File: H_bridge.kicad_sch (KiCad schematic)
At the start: 13 parts, among them M1 Motor_AC, Q1 AO3400A, Q2 AO3400A, Q3 AO3400A, Q4 AO3400A, U2 SLM2009, U3 SLM2009

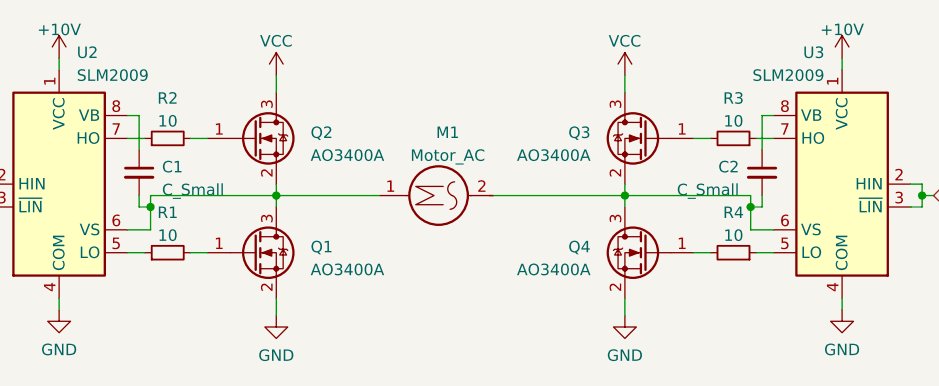
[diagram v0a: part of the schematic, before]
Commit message: mostek H, serva, SMPS
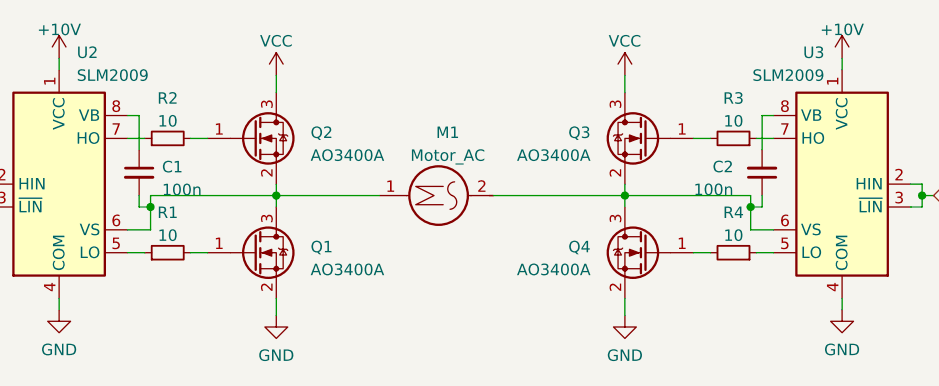
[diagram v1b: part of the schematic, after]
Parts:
- C1, C2: value C_Small -> 100n
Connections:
- net at M1.2, Q3.2 (S), Q4.3 (D)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: now also C2.1; no longer C2.2
- net at U3.8 (VB): now also C2.2; no longer C2.1
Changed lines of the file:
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@@
     )
   )
-  (symbol (lib_id "Device:C_Small") (at 172.085 83.82 0) (mirror y) (unit 1)
+  (symbol (lib_id "Device:C_Small") (at 172.085 83.82 0) (mirror x) (unit 1)
     (in_bom yes) (on_board yes) (dnp no) (fields_autoplaced)
-    (property "Reference" "C2" (at 169.545 83.1913 0)
-      (effects (font (size 1.27 1.27)) (justify left))
+    (property "Reference" "C2" (at 168.91 83.1786 0)
+      (effects (font (size 1.27 1.27)) (justify right))
     )
-    (property "Value" "C_Small" (at 169.545 85.7313 0)
-      (effects (font (size 1.27 1.27)) (justify left))
+    (property "Value" "100n" (at 168.91 85.7186 0)
+      (effects (font (size 1.27 1.27)) (justify right))
     )
     (property "Footprint" "" (at 172.085 83.82 0)
@@
       (effects (font (size 1.27 1.27)) (justify left))
     )
-    (property "Value" "C_Small" (at 105.41 85.7313 0)
+    (property "Value" "100n" (at 105.41 85.7313 0)
       (effects (font (size 1.27 1.27)) (justify left))
     )

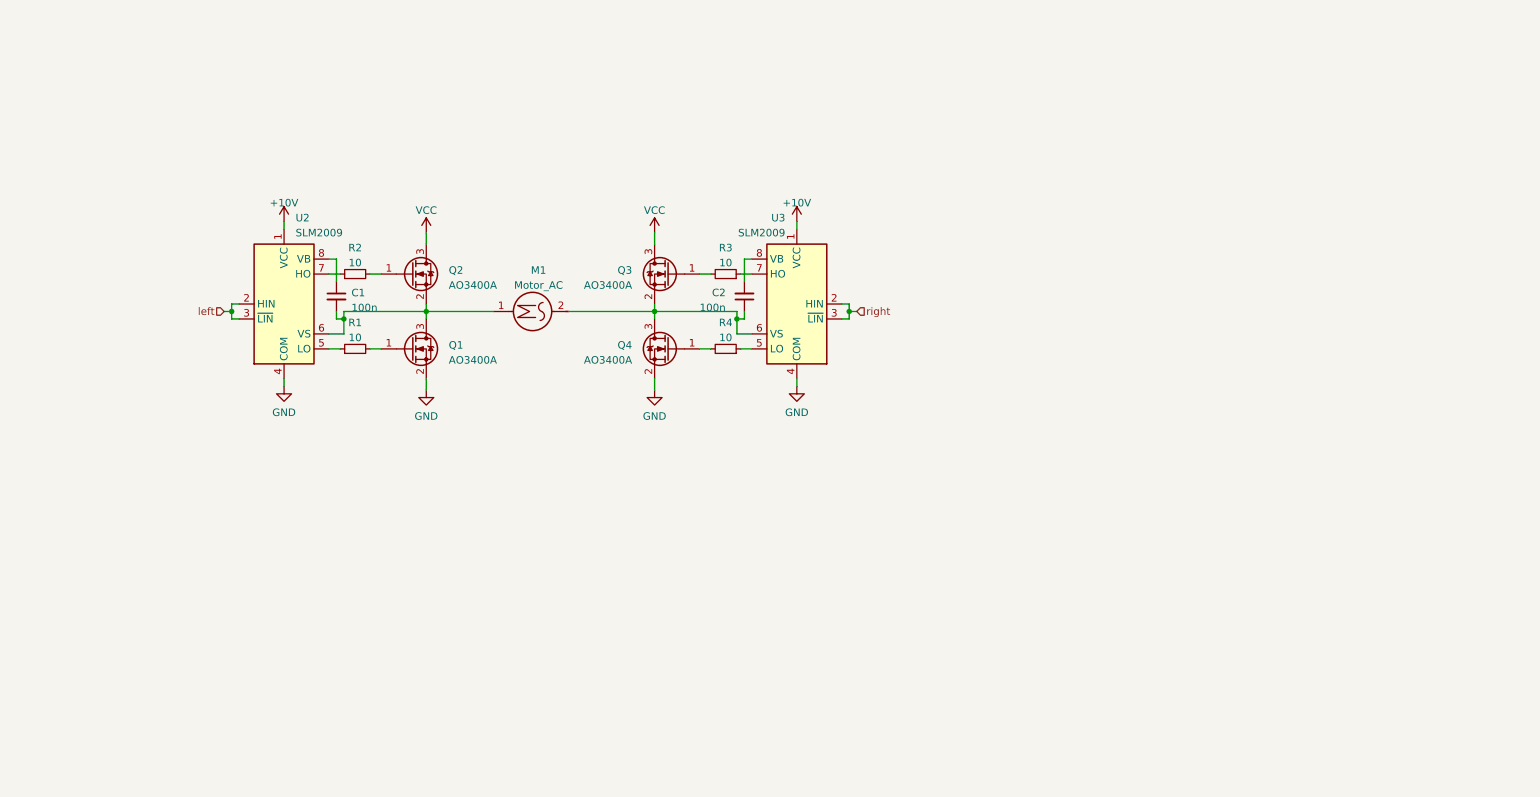
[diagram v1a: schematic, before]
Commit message: routing of H bridges and servo power pins
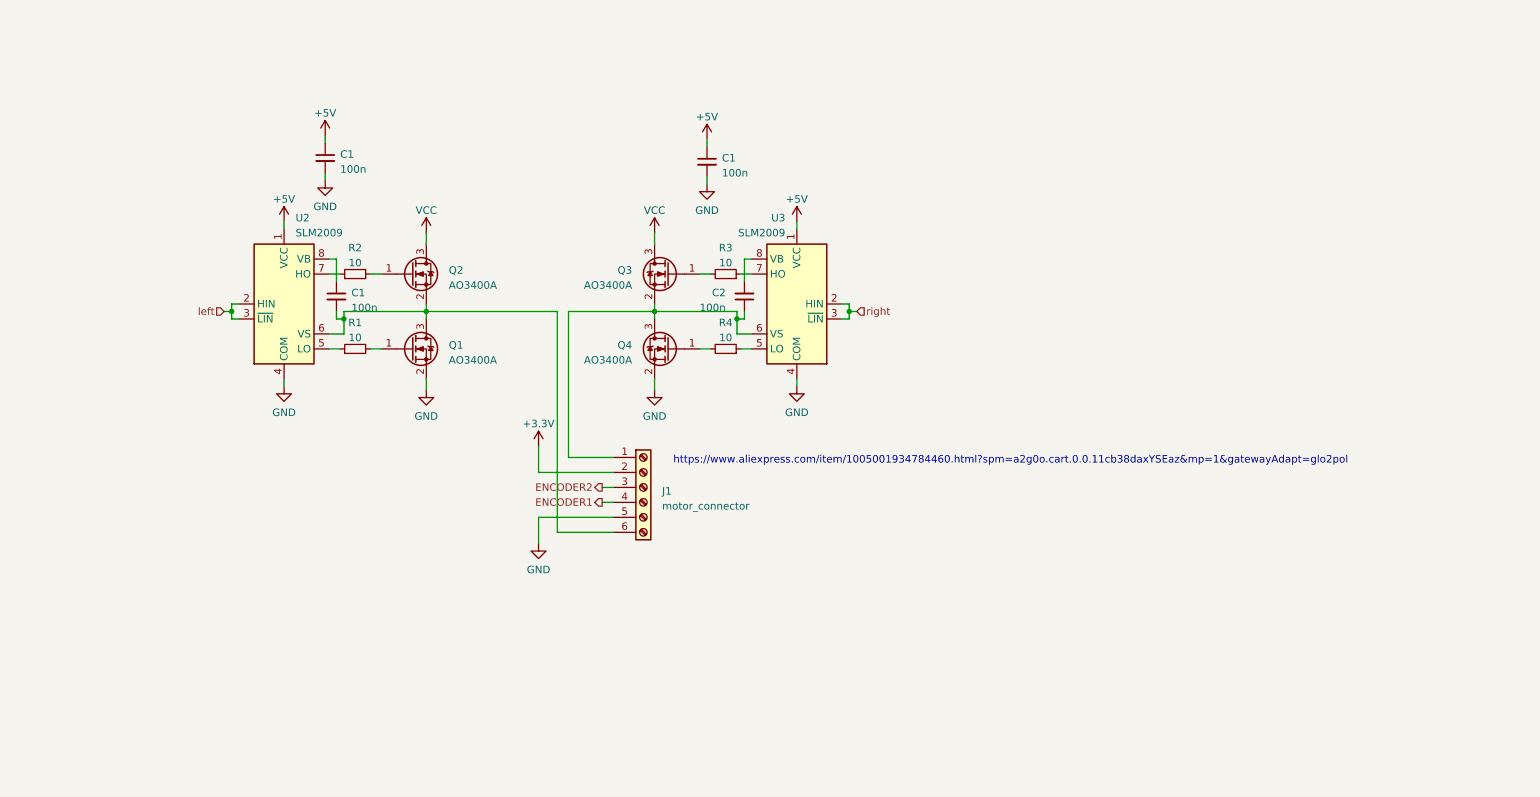
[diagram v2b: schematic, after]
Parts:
- removed M1: Motor_AC, symbol Motor:Motor_AC
- added C1 (x2): 100n, Capacitor_SMD:C_0603_1608Metric_Pad1.08x0.95mm_HandSolder, symbol Device:C_Small
- added J1: motor_connector, symbol Connector:Screw_Terminal_01x06
- C1, C2: footprint (none) -> Capacitor_SMD:C_0603_1608Metric_Pad1.08x0.95mm_HandSolder
- R1, R2, R3, R4: footprint (none) -> Resistor_SMD:R_0603_1608Metric_Pad0.98x0.95mm_HandSolder
- U2, U3: footprint (none) -> Package_SO:SOIC-8_3.9x4.9mm_P1.27mm
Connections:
- net GND: now also C1.2, C1.2, J1.5 (Pin_5)
- net at C1.2, Q1.3 (D), Q2.2 (S)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: now also J1.6 (Pin_6)
- net at C2.1, Q3.2 (S), Q4.3 (D)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: now also J1.1 (Pin_1)
- net +10V renamed +5V
- net +5V: now also C1.1, C1.1
- new net +3.3V: J1.2 (Pin_2)
- new net ENCODER1: J1.4 (Pin_4)
- new net ENCODER2: J1.3 (Pin_3)
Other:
- note added: "https://www.aliexpress.com/item/1005001934784460.html?spm=a2g0o.cart.0.0.11cb38daxYSEaz&mp=1&gatewayAdapt=glo2pol"

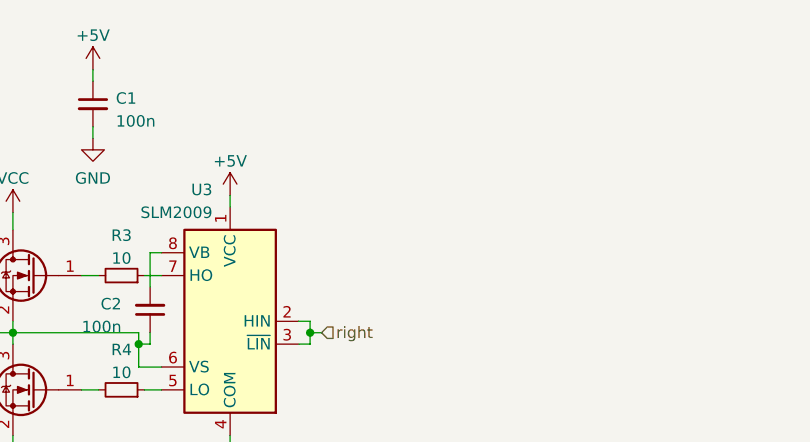
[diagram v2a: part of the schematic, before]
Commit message: more capacitance near motors 16x22uF total 3S->2S
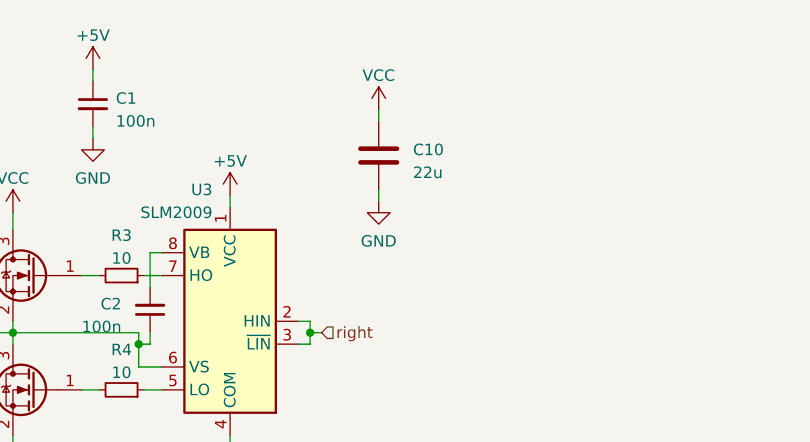
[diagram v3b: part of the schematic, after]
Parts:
- added C10: 22u, Capacitor_SMD:C_0805_2012Metric_Pad1.18x1.45mm_HandSolder, symbol Device:C
- J1: footprint (none) -> Connector_PinSocket_2.54mm:PinSocket_1x06_P2.54mm_Vertical
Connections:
- net GND: now also C10.2
- net VCC: now also C10.1
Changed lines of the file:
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@@
+    (stroke (width 0) (type default))
+  )
+  (wire (pts (xy 197.485 61.595) (xy 197.485 62.865))
     (stroke (width 0) (type default))
   )
@@
   )
   (wire (pts (xy 166.37 80.01) (xy 164.465 80.01))
+    (stroke (width 0) (type default))
+  )
+  (wire (pts (xy 197.485 70.485) (xy 197.485 71.755))
     (stroke (width 0) (type default))
   )
@@
       (effects (font (size 1.27 1.27)) (justify left))
     )
-    (property "Footprint" "" (at 154.94 116.205 0)
+    (property "Footprint" "Connector_PinSocket_2.54mm:PinSocket_1x06_P2.54mm_Vertical" (at 154.94 116.205 0)
       (effects (font (size 1.27 1.27)) hide)
     )
@@
     )
   )
+  (symbol (lib_id "Device:C") (at 197.485 66.675 0) (unit 1)
+    (in_bom yes) (on_board yes) (dnp no) (fields_autoplaced)
+    (property "Reference" "C10" (at 201.295 66.04 0)
+      (effects (font (size 1.27 1.27)) (justify left))
+    )
+    (property "Value" "22u" (at 201.295 68.58 0)
+      (effects (font (size 1.27 1.27)) (justify left))
+    )
+    (property "Footprint" "Capacitor_SMD:C_0805_2012Metric_Pad1.18x1.45mm_HandSolder" (at 198.4502 70.485 0)
+      (effects (font (size 1.27 1.27)) hide)
+    )
+    (property "Datasheet" "~" (at 197.485 66.675 0)
+      (effects (font (size 1.27 1.27)) hide)
+    )
+    (pin "1")
+    (pin "2")
+    (instances
+      (project "version_1"
+        (path "/23ba0750-4a55-4d50-828b-749cc0fbb8c8"
+          (reference "C10") (unit 1)
+        )
+        (path "/23ba0750-4a55-4d50-828b-749cc0fbb8c8/9789521c-7f58-473a-9dd2-6c6a71290f6c"
+          (reference "C15") (unit 1)
+        )
+        (path "/23ba0750-4a55-4d50-828b-749cc0fbb8c8/03ada194-765a-457e-8ab8-6dd2c4500630"
+          (reference "C35") (unit 1)
+        )
+        (path "/23ba0750-4a55-4d50-828b-749cc0fbb8c8/79f7122c-c2a5-4829-b847-ff54a5199600"
+          (reference "C36") (unit 1)
+        )
+        (path "/23ba0750-4a55-4d50-828b-749cc0fbb8c8/d2110296-333c-46f5-b5da-c8cbeafe02ed"
+          (reference "C37") (unit 1)
+        )
+        (path "/23ba0750-4a55-4d50-828b-749cc0fbb8c8/1b8f704b-b129-4c22-a423-d346d579d0e5"
+          (reference "C38") (unit 1)
+        )
+        (path "/23ba0750-4a55-4d50-828b-749cc0fbb8c8/0734ecc9-bf55-4847-b598-21bbdec71699"
+          (reference "C39") (unit 1)
+        )
+      )
+    )
+  )
   (symbol (lib_id "Transistor_FET:AO3400A") (at 159.385 80.01 0) (mirror y) (unit 1)
     (in_bom yes) (on_board yes) (dnp no) (fields_autoplaced)
@@
         (path "/23ba0750-4a55-4d50-828b-749cc0fbb8c8/0734ecc9-bf55-4847-b598-21bbdec71699"
           (reference "#PWR072") (unit 1)
+        )
+      )
+    )
+  )
+  (symbol (lib_id "power:GND") (at 197.485 71.755 0) (unit 1)
+    (in_bom yes) (on_board yes) (dnp no) (fields_autoplaced)
+    (property "Reference" "#PWR055" (at 197.485 78.105 0)
+      (effects (font (size 1.27 1.27)) hide)
+    )
+    (property "Value" "GND" (at 197.485 76.2 0)
+      (effects (font (size 1.27 1.27)))
+    )
+    (property "Footprint" "" (at 197.485 71.755 0)
+      (effects (font (size 1.27 1.27)) hide)
+    )
+    (property "Datasheet" "" (at 197.485 71.755 0)
+      (effects (font (size 1.27 1.27)) hide)
+    )
+    (pin "1")
+    (instances
+      (project "version_1"
+        (path "/23ba0750-4a55-4d50-828b-749cc0fbb8c8"
+          (reference "#PWR055") (unit 1)
+        )
+        (path "/23ba0750-4a55-4d50-828b-749cc0fbb8c8/9789521c-7f58-473a-9dd2-6c6a71290f6c"
+          (reference "#PWR066") (unit 1)
+        )
+        (path "/23ba0750-4a55-4d50-828b-749cc0fbb8c8/03ada194-765a-457e-8ab8-6dd2c4500630"
+          (reference "#PWR0117") (unit 1)
+        )
+        (path "/23ba0750-4a55-4d50-828b-749cc0fbb8c8/79f7122c-c2a5-4829-b847-ff54a5199600"
+          (reference "#PWR0119") (unit 1)
+        )
+        (path "/23ba0750-4a55-4d50-828b-749cc0fbb8c8/d2110296-333c-46f5-b5da-c8cbeafe02ed"
+          (reference "#PWR0121") (unit 1)
+        )
+        (path "/23ba0750-4a55-4d50-828b-749cc0fbb8c8/1b8f704b-b129-4c22-a423-d346d579d0e5"
+          (reference "#PWR0123") (unit 1)
+        )
+        (path "/23ba0750-4a55-4d50-828b-749cc0fbb8c8/0734ecc9-bf55-4847-b598-21bbdec71699"
+          (reference "#PWR0125") (unit 1)
         )
       )
@@
         )
       )
+    )
+  )
+  (symbol (lib_id "power:VCC") (at 197.485 61.595 0) (unit 1)
+    (in_bom yes) (on_board yes) (dnp no) (fields_autoplaced)
+    (property "Reference" "#PWR051" (at 197.485 65.405 0)
+      (effects (font (size 1.27 1.27)) hide)
+    )
+    (property "Value" "VCC" (at 197.485 57.785 0)
+      (effects (font (size 1.27 1.27)))
+    )
+    (property "Footprint" "" (at 197.485 61.595 0)
+      (effects (font (size 1.27 1.27)) hide)
+    )
+    (property "Datasheet" "" (at 197.485 61.595 0)
+      (effects (font (size 1.27 1.27)) hide)
+    )
+    (pin "1")
+    (instances
+      (project "version_1"
+        (path "/23ba0750-4a55-4d50-828b-749cc0fbb8c8"
+          (reference "#PWR051") (unit 1)
+        )
+        (path "/23ba0750-4a55-4d50-828b-749cc0fbb8c8/9789521c-7f58-473a-9dd2-6c6a71290f6c"
+          (reference "#PWR065") (unit 1)
+        )
+        (path "/23ba0750-4a55-4d50-828b-749cc0fbb8c8/03ada194-765a-457e-8ab8-6dd2c4500630"
+          (reference "#PWR0116") (unit 1)
+        )
+        (path "/23ba0750-4a55-4d50-828b-749cc0fbb8c8/79f7122c-c2a5-4829-b847-ff54a5199600"
+          (reference "#PWR0118") (unit 1)
+        )
+        (path "/23ba0750-4a55-4d50-828b-749cc0fbb8c8/d2110296-333c-46f5-b5da-c8cbeafe02ed"
+          (reference "#PWR0120") (unit 1)
+        )
+        (path "/23ba0750-4a55-4d50-828b-749cc0fbb8c8/1b8f704b-b129-4c22-a423-d346d579d0e5"
+          (reference "#PWR0122") (unit 1)
+        )
+        (path "/23ba0750-4a55-4d50-828b-749cc0fbb8c8/0734ecc9-bf55-4847-b598-21bbdec71699"
+          (reference "#PWR0124") (unit 1)
+        )
+      )

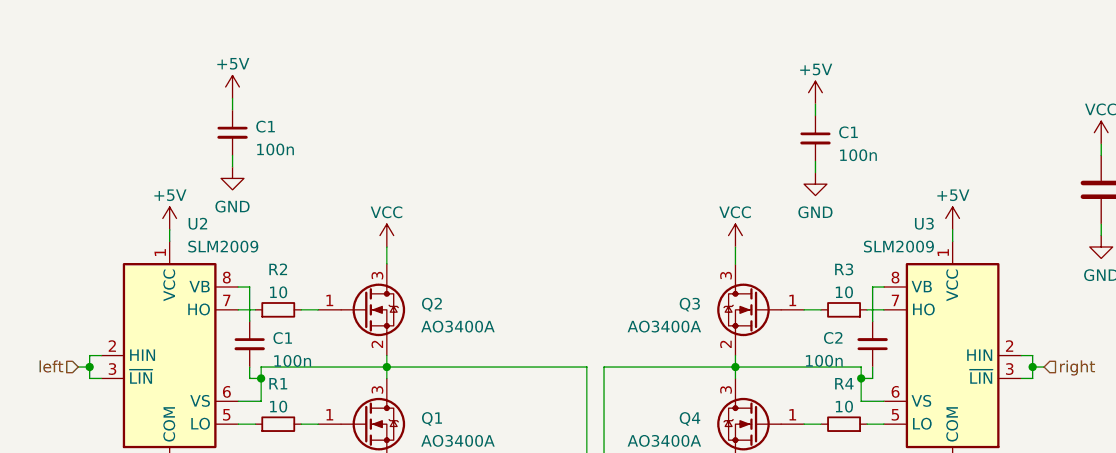
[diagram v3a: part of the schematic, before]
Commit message: new version of layout with diodes improved power routing a little bit
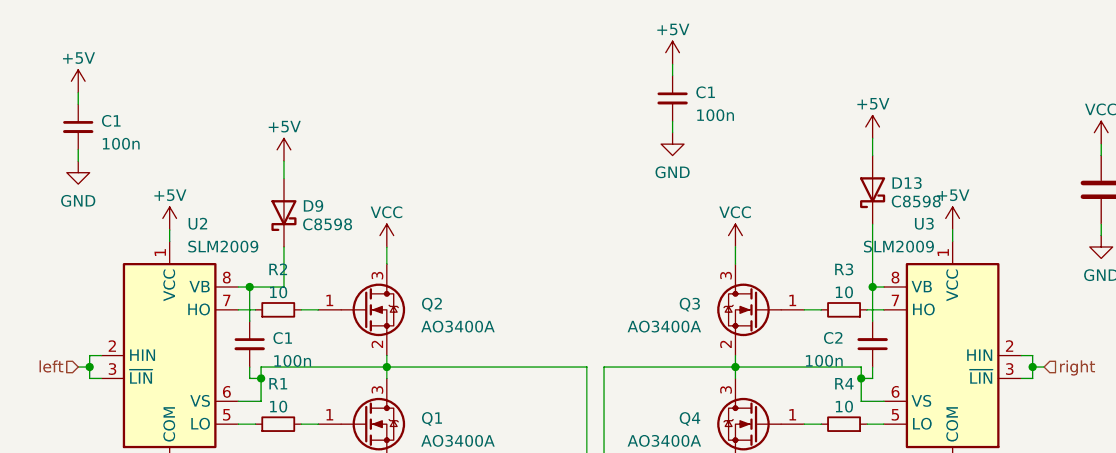
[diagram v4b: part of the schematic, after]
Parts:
- added D13, D9: C8598, Diode_SMD:D_SOD-123, symbol Device:D_Schottky
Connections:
- net +5V: now also D13.2 (A), D9.2 (A)
- net at C2.2, U3.8 (VB): now also D13.1 (K)
- net at C1.1, U2.8 (VB): now also D9.1 (K)
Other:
- moved on the sheet: C1

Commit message: added moany componaets
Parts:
- added C10 (x5): 22u, Capacitor_SMD:C_0805_2012Metric_Pad1.18x1.45mm_HandSolder, symbol Device:C
- added CN1: B6B-PH-K-S(LF)(SN), footprint:CONN-TH_B6B-PH-K-S, symbol B6B-PH-K-S(LF)(SN):B6B-PH-K-S(LF)(SN)
- added U13: DRV8870DDA, Package_SO:Texas_HTSOP-8-1EP_3.9x4.9mm_P1.27mm_EP2.95x4.9mm_Mask2.4x3.1mm_ThermalVias, symbol Driver_Motor:DRV8870DDA
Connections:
- net +3.3V: now also CN1.5
- net +5V: now also U13.4 (VREF)
- net GND: now also C10.2, C10.2, C10.2, C10.2, C10.2, U13.1 (GND), U13.7 (ISEN), U13.9 (GND)
- net VCC: now also C10.1, C10.1, C10.1, C10.1, C10.1, U13.5 (VM)
- net left: now also U13.3 (IN1)
- net right: now also U13.2 (IN2)
- new net: CN1.1, U13.8 (OUT2)
- new net: CN1.6, U13.6 (OUT1)
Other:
- note added: "C131342"

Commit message: some changes
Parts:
- removed C2: 100n, Capacitor_SMD:C_0603_1608Metric_Pad1.08x0.95mm_HandSolder, symbol Device:C_Small
- removed D13, D9: C8598, Diode_SMD:D_SOD-123, symbol Device:D_Schottky
- removed J1: motor_connector, Connector_PinSocket_2.54mm:PinSocket_1x06_P2.54mm_Vertical, symbol Connector:Screw_Terminal_01x06
- removed Q1, Q2, Q3, Q4: AO3400A, Package_TO_SOT_SMD:SOT-23, symbol Transistor_FET:AO3400A
- removed R1, R2, R3, R4: 10, Resistor_SMD:R_0603_1608Metric_Pad0.98x0.95mm_HandSolder, symbol Device:R_Small
- removed U2, U3: SLM2009, Package_SO:SOIC-8_3.9x4.9mm_P1.27mm, symbol Driver_FET:IR2103
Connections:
- net ENCODER1: now also CN1.3
- net ENCODER2: now also CN1.4
- net GND: now also C1.2, CN1.2
- net VCC: now also C1.1
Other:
- note added: "Need to flip?"
- note removed: "C131342"
- note removed: "https://www.aliexpress.com/item/1005001934784460.html?spm=a2g0o.cart.0.0.11cb38daxYSEaz&mp=1&gatewayAdapt=glo2pol"
- moved on the sheet: C1, C10, CN1, U13
